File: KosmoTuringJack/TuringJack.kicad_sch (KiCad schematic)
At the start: 10 parts, among them J1 Conn_01x10_Female

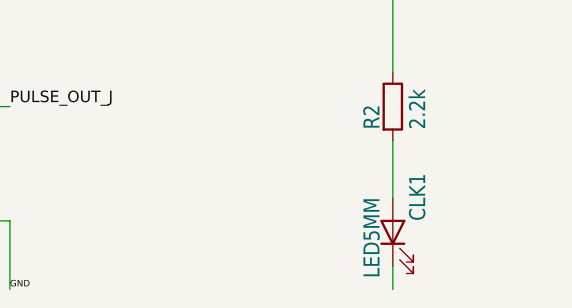
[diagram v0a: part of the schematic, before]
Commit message: fix #1 missing cathode connection of clock led
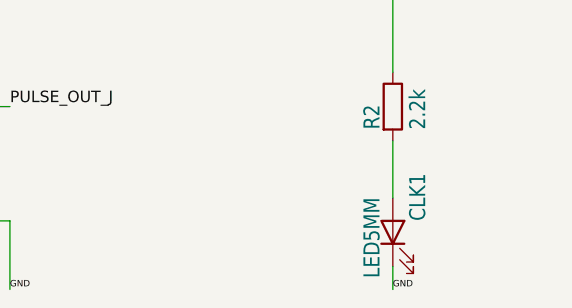
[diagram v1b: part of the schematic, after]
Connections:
- net GND: now also CLK1.1 (K)
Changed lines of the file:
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@@
     (effects (font (size 1.2446 1.2446)) (justify right bottom))
+  )
+  (label "GND" (at 147.32 158.115 0)
+    (effects (font (size 0.7112 0.7112)) (justify left bottom))
   )
   (label "GND" (at 156.21 76.835 180)

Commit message: move pulse out 1k resistor after the led, so it does not act as voltage divider, thanks @holmesrichards !
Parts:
- added R3: 1k, ao_tht:R_Axial_DIN0207_L6.3mm_D2.5mm_P10.16mm_Horizontal, symbol ao_symbols:R
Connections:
- net PULSE_OUT_J: now also R3.1; no longer PULSE_OUT1.T
- new net: PULSE_OUT1.T, R3.2
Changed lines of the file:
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@@
     (effects (font (size 1.27 1.27)) (justify left bottom))
   )
-  (label "PULSE_OUT_J" (at 156.21 79.375 180)
+  (label "PULSE_OUT_J" (at 148.59 79.375 180)
     (effects (font (size 1.27 1.27)) (justify right bottom))
   )
@@
     (pin "9")
   )
+  (symbol (lib_id "ao_symbols:R") (at 152.4 79.375 90) (unit 1)
+    (in_bom yes) (on_board yes)
+    (property "Reference" "R3" (id 0) (at 152.4 81.915 90))
+    (property "Value" "1k" (id 1) (at 152.4 79.375 90))
+    (property "Footprint" "ao_tht:R_Axial_DIN0207_L6.3mm_D2.5mm_P10.16mm_Horizontal" (id 2) (at 152.4 81.153 90)
+      (effects (font (size 1.27 1.27)) hide)
+    )
+    (property "Datasheet" "" (id 3) (at 152.4 79.375 0)
+      (effects (font (size 1.27 1.27)) hide)
+    )
+    (property "Vendor" "Tayda" (id 4) (at 152.4 79.375 0)
+      (effects (font (size 1.27 1.27)) hide)
+    )
+    (pin "1")
+    (pin "2")
+  )
   (symbol (lib_id "ao_symbols:LED_green") (at 147.32 151.765 90) (unit 1)
     (in_bom yes) (on_board yes)
@@
       (reference "R2") (unit 1) (value "2.2k") (footprint "ao_tht:R_Axial_DIN0207_L6.3mm_D2.5mm_P10.16mm_Horizontal")
     )
-  )
+    (path "/9f9126b0-dd1e-49be-922e-fd09297e0548"
+      (reference "R3") (unit 1) (value "1k") (footprint "ao_tht:R_Axial_DIN0207_L6.3mm_D2.5mm_P10.16mm_Horizontal")
+    )
+  )
